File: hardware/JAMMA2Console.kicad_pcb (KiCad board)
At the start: 2 copper layers, 118 x 87.8 mm, 67 parts, among them J1 Conn_02x28_JAMMA, J2 SCART-F, J3 DB15_Female_HighDensity, J4 Conn_Coaxial_x2, J5 DB15_Female, J6 DB15_Female, J7 DF1BZ-34DP-2.5DSA, U1 STM32F103V8Tx, U2 74LVC4245, U3 74LVC4245, U4 74LVC4245, U5 LM1881, U6 TL072

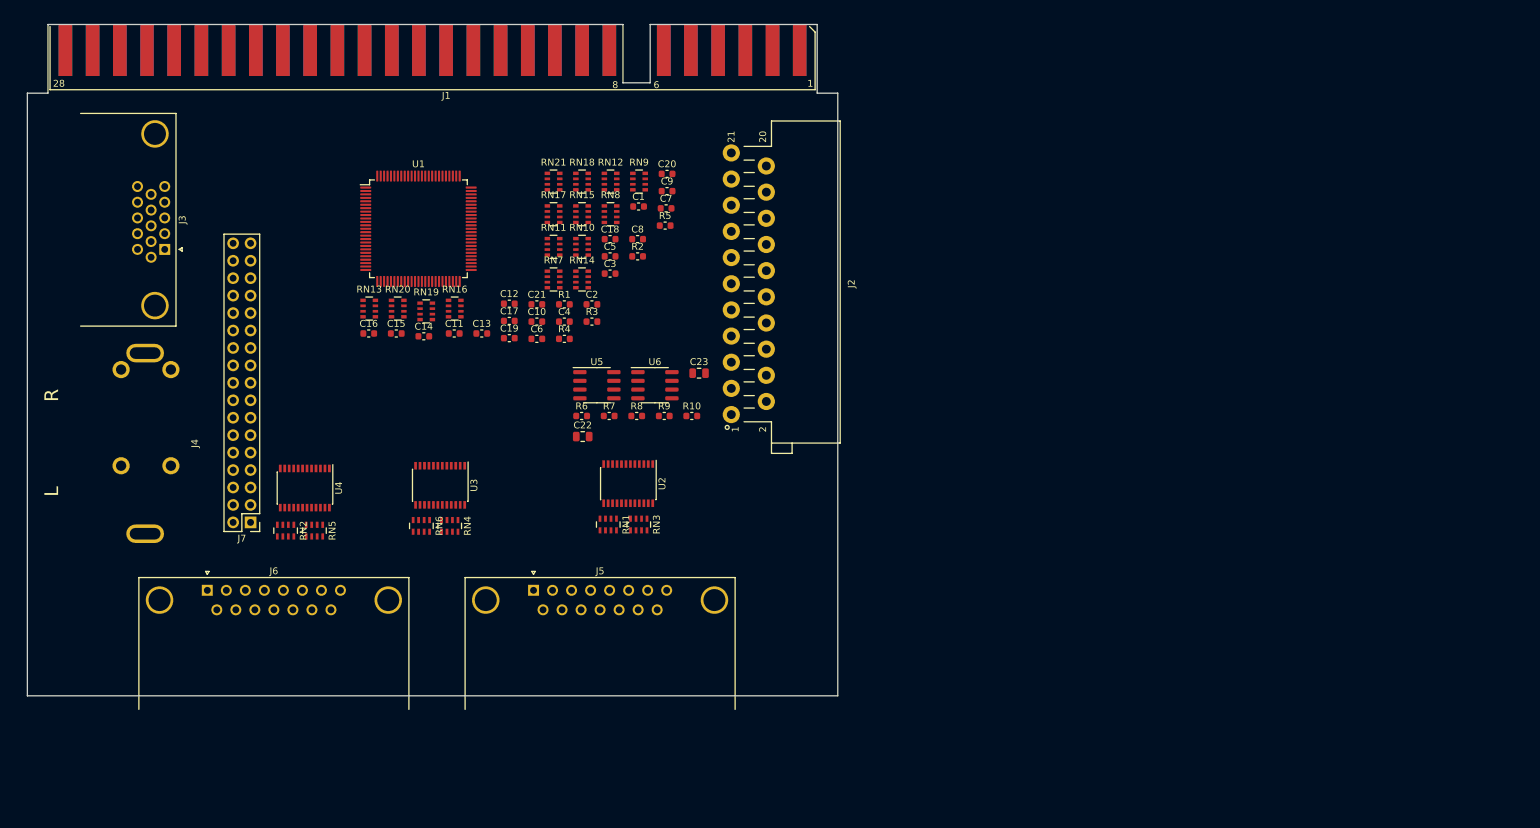
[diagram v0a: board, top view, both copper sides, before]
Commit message: More work on various schematic files, added footprint for the speaker out terminal connectors.
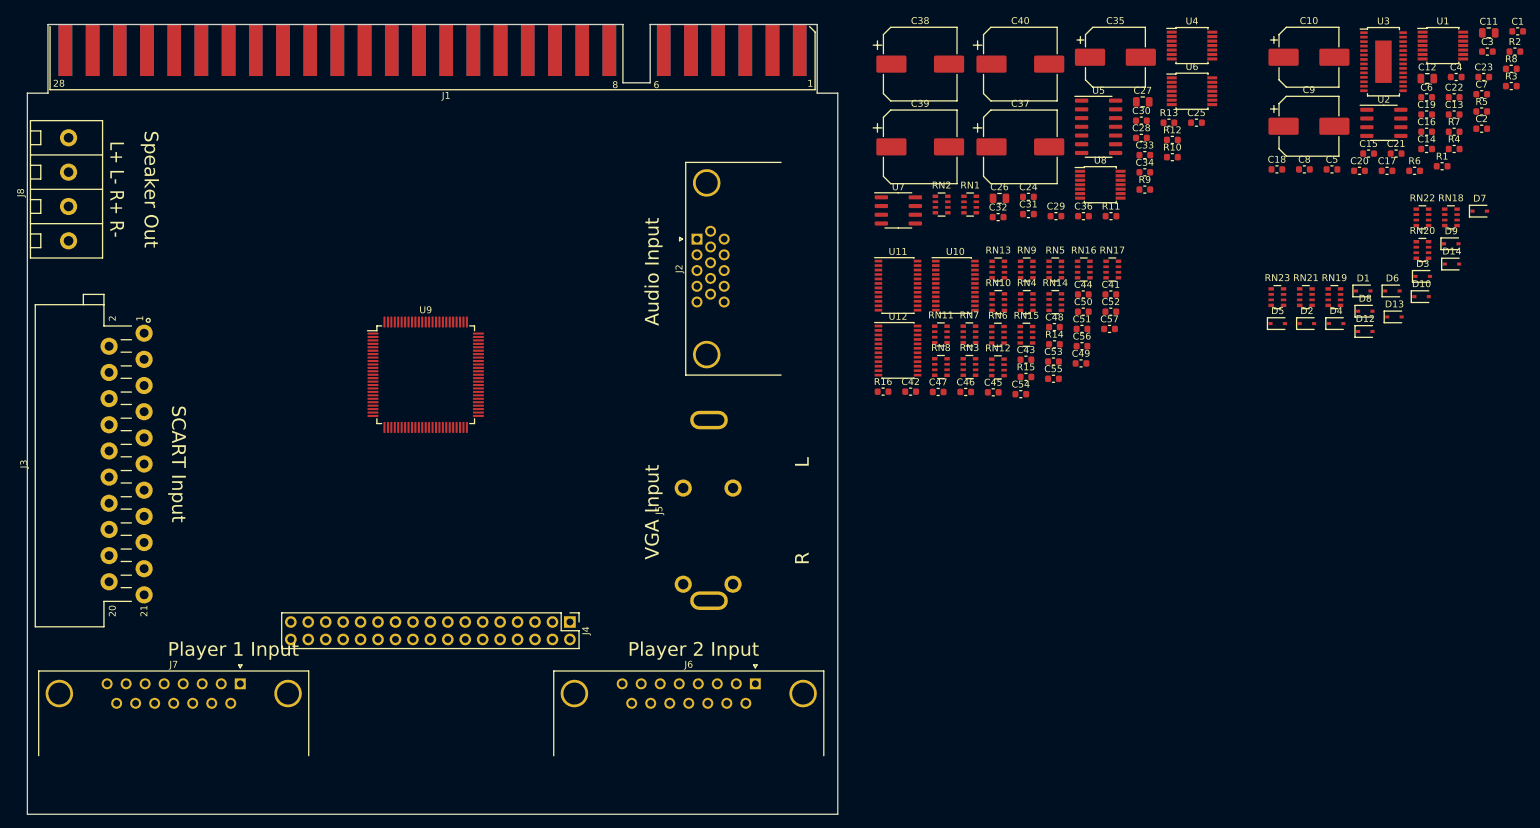
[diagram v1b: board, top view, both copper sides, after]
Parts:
- added C24: 100n, Capacitor_SMD:C_0603_1608Metric, F.Cu at (235.8, 69.3)
- added C25: 100n, Capacitor_SMD:C_0603_1608Metric, F.Cu at (260.2, 58.5)
- added C26: 10u, Capacitor_SMD:C_0805_2012Metric, F.Cu at (231.6, 69.6)
- added C27: 10u, Capacitor_SMD:C_0805_2012Metric, F.Cu at (252.4, 55.5)
- added C28: 100n, Capacitor_SMD:C_0603_1608Metric, F.Cu at (252.2, 60.8)
- added C29: 100n, Capacitor_SMD:C_0603_1608Metric, F.Cu at (239.8, 72.2)
- added C30: 100n, Capacitor_SMD:C_0603_1608Metric, F.Cu at (252.2, 58.2)
- added C31: 510p, Capacitor_SMD:C_0603_1608Metric, F.Cu at (235.8, 71.9)
- added C32: 100n, Capacitor_SMD:C_0603_1608Metric, F.Cu at (231.3, 72.3)
- added C33: 100n, Capacitor_SMD:C_0603_1608Metric, F.Cu at (252.7, 63.3)
- added C34: 100n, Capacitor_SMD:C_0603_1608Metric, F.Cu at (252.7, 65.8)
- added C35: 100u, Capacitor_SMD:CP_Elec_8x10.5, F.Cu at (248.4, 49.0)
- added C36: 100n, Capacitor_SMD:C_0603_1608Metric, F.Cu at (243.8, 72.2)
- added C37: 330u, Capacitor_SMD:CP_Elec_10x10.5, F.Cu at (234.6, 62.1)
- added C38: 330u, Capacitor_SMD:CP_Elec_10x10.5, F.Cu at (220.0, 50.0)
- added C39: 330u, Capacitor_SMD:CP_Elec_10x10.5, F.Cu at (220.0, 62.1)
- added C40: 330u, Capacitor_SMD:CP_Elec_10x10.5, F.Cu at (234.6, 50.0)
- added C41: 10u, Capacitor_SMD:C_0603_1608Metric, F.Cu at (247.8, 83.6)
- added C42: 100n, Capacitor_SMD:C_0603_1608Metric, F.Cu at (218.6, 97.7)
- added C43: 100n, Capacitor_SMD:C_0603_1608Metric, F.Cu at (235.4, 93.1)
- added C44: 100n, Capacitor_SMD:C_0603_1608Metric, F.Cu at (243.8, 83.6)
- added C45: 100n, Capacitor_SMD:C_0603_1608Metric, F.Cu at (230.6, 97.8)
- added C46: 100n, Capacitor_SMD:C_0603_1608Metric, F.Cu at (226.6, 97.8)
- added C47: 100n, Capacitor_SMD:C_0603_1608Metric, F.Cu at (222.6, 97.8)
- added C48: 10u, Capacitor_SMD:C_0603_1608Metric, F.Cu at (239.6, 88.3)
- added C49: 100n, Capacitor_SMD:C_0603_1608Metric, F.Cu at (243.4, 93.6)
- added C50: 100n, Capacitor_SMD:C_0603_1608Metric, F.Cu at (243.8, 86.1)
- added C51: 100n, Capacitor_SMD:C_0603_1608Metric, F.Cu at (243.6, 88.6)
- added C52: 100n, Capacitor_SMD:C_0603_1608Metric, F.Cu at (247.8, 86.1)
- added C53: 100n, Capacitor_SMD:C_0603_1608Metric, F.Cu at (239.4, 93.3)
- added C54: 100n, Capacitor_SMD:C_0603_1608Metric, F.Cu at (234.7, 98.1)
- added C55: 100n, Capacitor_SMD:C_0603_1608Metric, F.Cu at (239.4, 95.8)
- added C56: 100n, Capacitor_SMD:C_0603_1608Metric, F.Cu at (243.6, 91.1)
- added C57: 100n, Capacitor_SMD:C_0603_1608Metric, F.Cu at (247.6, 88.6)
- added D1: LESD3Z5.0CMT1G, Diode_SMD:D_SOD-323, F.Cu at (284.5, 83.0)
- added D10: LESD3Z5.0CMT1G, Diode_SMD:D_SOD-323, F.Cu at (293.0, 83.9)
- added D12: LESD3Z5.0CMT1G, Diode_SMD:D_SOD-323, F.Cu at (284.8, 89.0)
- added D13: LESD3Z5.0CMT1G, Diode_SMD:D_SOD-323, F.Cu at (289.1, 86.8)
- added D14: LESD3Z5.0CMT1G, Diode_SMD:D_SOD-323, F.Cu at (297.4, 79.1)
- added D2: LESD3Z5.0CMT1G, Diode_SMD:D_SOD-323, F.Cu at (276.3, 87.8)
- added D3: LESD3Z5.0CMT1G, Diode_SMD:D_SOD-323, F.Cu at (293.2, 80.9)
- added D4: LESD3Z5.0CMT1G, Diode_SMD:D_SOD-323, F.Cu at (280.6, 87.8)
- added D5: LESD3Z5.0CMT1G, Diode_SMD:D_SOD-323, F.Cu at (272.1, 87.8)
- added D6: LESD3Z5.0CMT1G, Diode_SMD:D_SOD-323, F.Cu at (288.8, 83.0)
- added D7: LESD3Z5.0CMT1G, Diode_SMD:D_SOD-323, F.Cu at (301.5, 71.4)
- added D8: LESD3Z5.0CMT1G, Diode_SMD:D_SOD-323, F.Cu at (284.8, 86.0)
- added D9: LESD3Z5.0CMT1G, Diode_SMD:D_SOD-323, F.Cu at (297.3, 76.2)
- added J8: Conn_01x04, Console2JAMMA:PhoenixContact_PTS_1,5_4-5_1x4_P5.00mm_Horizontal, F.Cu at (96.0, 68.2)
- added R11: 620, Resistor_SMD:R_0603_1608Metric, F.Cu at (247.8, 72.2)
- added R12: 680k, Resistor_SMD:R_0603_1608Metric, F.Cu at (256.7, 61.1)
- added R13: 10K, Resistor_SMD:R_0603_1608Metric, F.Cu at (256.2, 58.5)
- added R14: 10k, Resistor_SMD:R_0603_1608Metric, F.Cu at (239.6, 90.8)
- added R15: 10k, Resistor_SMD:R_0603_1608Metric, F.Cu at (235.4, 95.6)
- added R16: 10k, Resistor_SMD:R_0603_1608Metric, F.Cu at (214.6, 97.7)
- added RN22: 4K7, Resistor_SMD:R_Array_Convex_4x0603, F.Cu at (293.1, 72.3)
- added RN23: 4K7, Resistor_SMD:R_Array_Convex_4x0603, F.Cu at (272.0, 84.0)
- added U10: 74LVC4245, Package_SO:TSSOP-24_4.4x7.8mm_P0.65mm, F.Cu at (225.1, 82.3)
- added U11: 74LVC4245, Package_SO:TSSOP-24_4.4x7.8mm_P0.65mm, F.Cu at (216.8, 82.3)
- added U12: 74LVC4245, Package_SO:TSSOP-24_4.4x7.8mm_P0.65mm, F.Cu at (216.8, 91.7)
- added U7: LM1881, Package_SO:SOIC-8_3.9x4.9mm_P1.27mm, F.Cu at (216.8, 71.3)
- added U8: THS7375, Package_SO:TSSOP-14_4.4x5mm_P0.65mm, F.Cu at (246.2, 67.6)
- added U9: STM32F103V8Tx, Package_QFP:LQFP-100_14x14mm_P0.5mm, F.Cu at (148.0, 95.2)
- C1: value 510p -> 1u0
- C10, C9: value 100n -> 100u; footprint Capacitor_SMD:C_0603_1608Metric -> Capacitor_SMD:CP_Elec_8x10.5
- C11: value 100n -> 10u; footprint Capacitor_SMD:C_0603_1608Metric -> Capacitor_SMD:C_0805_2012Metric
- C12: footprint Capacitor_SMD:C_0603_1608Metric -> Capacitor_SMD:C_0805_2012Metric
- C15, C16, C19, C2, C3, C6, C7: value 100n -> 1u0
- C17, C18: value 100n -> 1n0
- C20, C21, C4, C8: value 100n -> 10n
- C22, C23: value 10u -> 10n; footprint Capacitor_SMD:C_0805_2012Metric -> Capacitor_SMD:C_0603_1608Metric
- C5: value 10u -> 1u0
- J2: value SCART-F -> DB15_Female_HighDensity; footprint Console2JAMMA:Conn_SCART_Female -> Connector_Dsub:DSUB-15-HD_Female_Horizontal_P2.29x1.98mm_EdgePinOffset8.35mm_Housed_MountingHolesOffset10.89mm
- J3: value DB15_Female_HighDensity -> SCART-F; footprint Connector_Dsub:DSUB-15-HD_Female_Horizontal_P2.29x1.98mm_EdgePinOffset8.35mm_Housed_MountingHolesOffset10.89mm -> Console2JAMMA:Conn_SCART_Female
- J4: value Conn_Coaxial_x2 -> DF1BZ-34DP-2.5DSA; footprint Console2JAMMA:RCA_Switchchraft_Dual -> Connector_PinHeader_2.54mm:PinHeader_2x17_P2.54mm_Vertical
- J5: value DB15_Female -> Conn_Coaxial_x2; footprint Connector_Dsub:DSUB-15_Male_Horizontal_P2.77x2.84mm_EdgePinOffset14.56mm_Housed_MountingHolesOffset15.98mm -> Console2JAMMA:RCA_Switchchraft_Dual
- J6: footprint Connector_Dsub:DSUB-15_Male_Horizontal_P2.77x2.84mm_EdgePinOffset14.56mm_Housed_MountingHolesOffset15.98mm -> Connector_Dsub:DSUB-15_Female_Horizontal_P2.77x2.84mm_EdgePinOffset7.70mm_Housed_MountingHolesOffset9.12mm
- J7: value DF1BZ-34DP-2.5DSA -> DB15_Female; footprint Connector_PinHeader_2.54mm:PinHeader_2x17_P2.54mm_Vertical -> Connector_Dsub:DSUB-15_Female_Horizontal_P2.77x2.84mm_EdgePinOffset7.70mm_Housed_MountingHolesOffset9.12mm
- R1: value 620 -> R_Small
- R10, R9: value 100K -> 4K7
- R2: value 680k -> R_Small
- R3, R4: value 10k -> 100K
- R5: value 10k -> 47K
- R8: value 47K -> 10K
- RN1, RN2: value 100R -> 75R; footprint Resistor_SMD:R_Array_Concave_4x0603 -> Resistor_SMD:R_Array_Convex_4x0603
- RN18, RN19, RN20, RN21: value 10k -> 4K7
- RN3, RN4, RN5, RN6: value 100R -> 10k; footprint Resistor_SMD:R_Array_Concave_4x0603 -> Resistor_SMD:R_Array_Convex_4x0603
- U1: value STM32F103V8Tx -> 74HC4053; footprint Package_QFP:LQFP-100_14x14mm_P0.5mm -> Package_SO:TSSOP-14_4.4x5mm_P0.65mm
- U2: value 74LVC4245 -> TL072; footprint Package_SO:TSSOP-24_4.4x7.8mm_P0.65mm -> Package_SO:SOIC-8_3.9x4.9mm_P1.27mm
- U3: value 74LVC4245 -> IS31AP2110; footprint Package_SO:TSSOP-24_4.4x7.8mm_P0.65mm -> Package_SO:TSSOP-28-1EP_4.4x9.7mm_P0.65mm
- U4: value 74LVC4245 -> 74HC4053; footprint Package_SO:TSSOP-24_4.4x7.8mm_P0.65mm -> Package_SO:TSSOP-14_4.4x5mm_P0.65mm
- U5: value LM1881 -> 74HC86; footprint Package_SO:SOIC-8_3.9x4.9mm_P1.27mm -> Package_SO:SOIC-14_3.9x8.7mm_P1.27mm
- U6: value TL072 -> 74HC4053; footprint Package_SO:SOIC-8_3.9x4.9mm_P1.27mm -> Package_SO:TSSOP-14_4.4x5mm_P0.65mm
- moved C11 156.9 mm to (302.8, 45.5)
- moved C16 156.8 mm to (293.7, 59.9)
- moved U1 151.5 mm to (296.1, 47.3)
- moved U3 150.6 mm to (287.5, 49.7), turned to 0 degrees
- moved RN20 149.4 mm to (293.1, 77.1)
- moved C14 148.5 mm to (293.7, 62.4)
- moved C13 145.1 mm to (297.8, 57.4)
- moved U4 144.4 mm to (259.6, 47.3), turned to 0 degrees
- moved C15 144.0 mm to (285.3, 63.0)
- moved R3 138.2 mm to (306.1, 53.2)
- moved C12 137.6 mm to (293.8, 52.1)
- moved C19 137.5 mm to (293.7, 57.4)
- moved R8 137.0 mm to (306.1, 50.7)
- moved C22 136.2 mm to (297.8, 54.9)
- moved C4 134.7 mm to (298.1, 51.9)
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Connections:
- net /Audio_R renamed /Speaker_R-
- net /P1P2_Shifter_DIR renamed Net-(U3-Pad2)
- net Net-(U1-Pad9) renamed /Audio/Audio_Select_Mono
- C1 pad 2: GND -> /Audio/EXT_Audio_L
- C10 pad 1: +3V3 -> +12V
- C11 pad 1: +3V3 -> Net-(C11-Pad1)
- C11 pad 2: GND -> /Audio/Audio_L
- C12 pad 1: +3V3 -> Net-(C12-Pad1)
- C12 pad 2: GND -> /Audio/Audio_R
- C13 pad 1: +3V3 -> +12V
- C14 pad 1: +3V3 -> +12V
- C15 pad 1: +3V3 -> Net-(C15-Pad1)
- C16 pad 1: VCC -> Net-(C16-Pad1)
- C17 pad 1: VCC -> +12V
- C18 pad 1: VCC -> +12V
- C19 pad 1: VCC -> +12V
- C2 pad 2: Net-(C1-Pad1) -> /Audio/EXT_Audio_R
- C20 pad 1: VCC -> /Speaker_JAMMA+
- C21 pad 1: VCC -> GND
- C21 pad 2: GND -> /Speaker_JAMMA-
- C22 pad 1: Net-(C22-Pad1) -> /Speaker_R+
- C22 pad 2: /Audio_L -> GND
- C23 pad 1: Net-(C23-Pad1) -> GND
- C3 pad 2: GND -> /Audio/Audio_Mono
- C5 pad 1: +3V3 -> Net-(C5-Pad1)
- C5 pad 2: GND -> /Audio/SCART_Audio_L
- C6 pad 1: +3V3 -> Net-(C6-Pad1)
- C6 pad 2: GND -> /Audio/SCART_Audio_R
- C7 pad 1: +3V3 -> Net-(C7-Pad1)
- C7 pad 2: GND -> /Audio/Audio_L
- C8 pad 1: +3V3 -> -5V
- C9 pad 1: +3V3 -> +12V
- J1 pad 10: /Speaker_R -> /Speaker_JAMMA+
- J1 pad L: /Speaker_L -> /Speaker_JAMMA-
- J2 pad 1: Net-(J2-Pad1) -> /VGA_Red
- J2 pad 10: Net-(J2-Pad10) -> GND
- J2 pad 11: /SCART_Green -> Net-(J2-Pad11)
- J2 pad 12: Net-(J2-Pad12) -> /VGA_SDA
- J2 pad 13: GND -> /VGA_HSYNC
- J2 pad 14: GND -> /VGA_VSYNC
- J2 pad 15: /SCART_Red -> /VGA_SCK
- J2 pad 2: /SCART_Audio_R -> /VGA_Green
- J2 pad 3: Net-(J2-Pad3) -> /VGA_Blue
- J2 pad 4: GND -> Net-(J2-Pad4)
- J2 pad 6: /SCART_Audio_L -> GND
- J2 pad 7: /SCART_Blue -> GND
- J2 pad 8: /SWITCH -> GND
- J2 pad 9: GND -> Net-(J2-Pad9)
- J3 pad 1: /VGA_Red -> Net-(J3-Pad1)
- J3 pad 10: GND -> Net-(J3-Pad10)
- J3 pad 11: Net-(J3-Pad11) -> /SCART_Green
- J3 pad 12: /VGA_SDA -> Net-(J3-Pad12)
- J3 pad 13: /VGA_HSYNC -> GND
- J3 pad 14: /VGA_VSYNC -> GND
- J3 pad 15: /VGA_SCK -> /SCART_Red
- J3 pad 2: /VGA_Green -> /SCART_Audio_R
- J3 pad 3: /VGA_Blue -> Net-(J3-Pad3)
- J3 pad 4: Net-(J3-Pad4) -> GND
- J3 pad 6: GND -> /SCART_Audio_L
- J3 pad 7: GND -> /SCART_Blue
- J3 pad 8: GND -> /SCART_Switch
- J3 pad 9: Net-(J3-Pad9) -> GND
- J4 pad 3: GND -> Net-(J4-Pad3)
- J5 pad 1: GND -> /EXT_Audio_L
- J5 pad 2: Net-(J5-Pad2) -> /EXT_Audio_R
- J5 pad 3: Net-(J5-Pad3) -> GND
- J6 pad 1: GND -> /Digital I/O/VCC
- J6 pad 15: Net-(J6-Pad15) -> GND
- J6 pad 8: VCC -> GND
- J6 pad 9: GND -> Net-(J6-Pad9)
- J7 pad 1: Net-(J7-Pad1) -> /Digital I/O/VCC
- J7 pad 15: /P1_HK -> GND
- J7 pad 8: Net-(J7-Pad8) -> GND
- J7 pad 9: /P2_HK -> Net-(J7-Pad9)
- R1 pad 1: Net-(C1-Pad1) -> +12V
- R1 pad 2: /SCART_COMP -> Net-(R1-Pad2)
- R10 pad 1: /Audio_Mono -> Net-(C27-Pad1)
- R10 pad 2: Net-(R10-Pad2) -> /Video/VGA_VSYNC
- R2 pad 1: Net-(C3-Pad1) -> Net-(R1-Pad2)
- R3 pad 1: GND -> Net-(R3-Pad1)
- R3 pad 2: Net-(R3-Pad2) -> Net-(C11-Pad1)
- R4 pad 1: GND -> Net-(R3-Pad1)
- R4 pad 2: Net-(R4-Pad2) -> Net-(C12-Pad1)
- R5 pad 1: GND -> Net-(R5-Pad1)
- R5 pad 2: Net-(R5-Pad2) -> Net-(R3-Pad1)
- R6 pad 2: Net-(C22-Pad1) -> Net-(R5-Pad1)
- R7 pad 1: Net-(R6-Pad1) -> Net-(R7-Pad1)
- R7 pad 2: Net-(C23-Pad1) -> Net-(R6-Pad1)
- R8 pad 1: Net-(R8-Pad1) -> /Audio/Audio_Mono
- R8 pad 2: Net-(R6-Pad1) -> Net-(R7-Pad1)
- R9 pad 1: Net-(R10-Pad2) -> Net-(C26-Pad1)
- R9 pad 2: Net-(R8-Pad1) -> /Video/VGA_HSYNC
- RN1 pad 1: Net-(RN1-Pad1) -> GND
- RN1 pad 2: Net-(RN1-Pad2) -> GND
- RN1 pad 3: Net-(RN1-Pad3) -> GND
- RN1 pad 4: Net-(RN1-Pad4) -> GND
- RN1 pad 5: Net-(J5-Pad4) -> /Video/Video_CSYNC
- RN1 pad 6: Net-(J5-Pad12) -> /Video/Video_Blue
- RN1 pad 7: Net-(J5-Pad5) -> /Video/Video_Green
- RN1 pad 8: Net-(J5-Pad13) -> /Video/Video_Red
- RN10 pad 1: /P1_HK -> /P2_HK
- RN10 pad 2: /P1_MK -> /P2_MK
- RN10 pad 3: /P1_LK -> /P2_LK
- RN11 pad 1: /Coin_B -> Net-(RN11-Pad1)
- RN11 pad 2: /P2_Start -> Net-(RN11-Pad2)
- RN11 pad 3: /P2_Up -> Net-(RN11-Pad3)
- RN11 pad 4: /P2_Down -> Net-(RN11-Pad4)
- RN11 pad 5: Net-(RN11-Pad5) -> /Digital I/O/P1_Button4
- RN11 pad 6: Net-(RN11-Pad6) -> /Digital I/O/P1_Button3
- RN11 pad 7: Net-(RN11-Pad7) -> /Digital I/O/P1_Button2
- RN11 pad 8: Net-(RN11-Pad8) -> /Digital I/O/P1_Button1
- RN12 pad 1: /P2_Left -> Net-(RN12-Pad1)
- RN12 pad 2: /P2_Right -> Net-(RN12-Pad2)
- RN12 pad 3: /P2_A -> Net-(RN12-Pad3)
- RN12 pad 4: /P2_B -> Net-(RN12-Pad4)
- RN12 pad 5: Net-(RN12-Pad5) -> /Digital I/O/P1_Button8
- RN12 pad 6: Net-(RN12-Pad6) -> /Digital I/O/P1_Button7
- RN12 pad 7: Net-(RN12-Pad7) -> /Digital I/O/P1_Button6
- RN12 pad 8: Net-(RN12-Pad8) -> /Digital I/O/P1_Button5
- RN13 pad 1: /P2_C -> Net-(RN13-Pad1)
- RN13 pad 2: /P2_X -> Net-(RN13-Pad2)
- RN13 pad 3: /P2_Y -> Net-(RN13-Pad3)
- RN13 pad 4: /P2_Z -> Net-(RN13-Pad4)
- RN13 pad 5: Net-(RN13-Pad5) -> /Digital I/O/P1_Button12
- RN13 pad 6: Net-(RN13-Pad6) -> /Digital I/O/P1_Button11
- RN13 pad 7: Net-(RN13-Pad7) -> /Digital I/O/P1_Button10
- RN13 pad 8: Net-(RN13-Pad8) -> /Digital I/O/P1_Button9
- RN14 pad 1: /P2_HK -> Net-(RN14-Pad1)
- RN14 pad 2: /P2_MK -> Net-(RN14-Pad2)
- RN14 pad 3: /P2_LK -> Net-(RN14-Pad3)
- RN14 pad 4: GND -> Net-(RN14-Pad4)
- RN14 pad 5: Net-(RN14-Pad5) -> GND
- RN14 pad 6: Net-(RN14-Pad6) -> /Digital I/O/P2_Shifter_DIR
- RN14 pad 7: Net-(RN14-Pad7) -> /Digital I/O/P1&P2_Shifter_DIR
- RN14 pad 8: Net-(RN14-Pad8) -> /Digital I/O/P1_Shifter_DIR
- RN15 pad 5: /P1_Button4 -> /Digital I/O/P2_Button4
- RN15 pad 6: /P1_Button3 -> /Digital I/O/P2_Button3
- RN15 pad 7: /P1_Button2 -> /Digital I/O/P2_Button2
- RN15 pad 8: /P1_Button1 -> /Digital I/O/P2_Button1
- RN16 pad 5: /P1_Button8 -> /Digital I/O/P2_Button8
- RN16 pad 6: /P1_Button7 -> /Digital I/O/P2_Button7
- RN16 pad 7: /P1_Button6 -> /Digital I/O/P2_Button6
- RN16 pad 8: /P1_Button5 -> /Digital I/O/P2_Button5
- RN17 pad 5: /P1_Button12 -> /Digital I/O/P2_Button12
- RN17 pad 6: /P1_Button11 -> /Digital I/O/P2_Button11
- RN17 pad 7: /P1_Button10 -> /Digital I/O/P2_Button10
- RN17 pad 8: /P1_Button9 -> /Digital I/O/P2_Button9
- RN18 pad 1: Net-(RN18-Pad1) -> /Digital I/O/P1_1
- RN18 pad 2: Net-(RN18-Pad2) -> /Digital I/O/P1_2
- RN18 pad 3: Net-(RN18-Pad3) -> /Digital I/O/P1_3
- RN18 pad 4: Net-(RN18-Pad4) -> /Digital I/O/P1_4
- RN18 pad 5: GND -> Net-(J6-Pad3)
- RN18 pad 6: /P2_Shifter_DIR -> Net-(J6-Pad10)
- RN18 pad 7: /P1&P2_Shifter_DIR -> Net-(J6-Pad2)
- RN18 pad 8: /P1_Shifter_DIR -> Net-(J6-Pad9)
- RN19 pad 1: Net-(RN19-Pad1) -> /Digital I/O/P1_5
- RN19 pad 2: Net-(RN19-Pad2) -> /Digital I/O/P1_6
- RN19 pad 3: Net-(RN19-Pad3) -> /Digital I/O/P1_7
- RN19 pad 4: Net-(RN19-Pad4) -> /Digital I/O/P1_8
- RN19 pad 5: /P2_Button4 -> Net-(J6-Pad5)
- RN19 pad 6: /P2_Button3 -> Net-(J6-Pad12)
- RN19 pad 7: /P2_Button2 -> Net-(J6-Pad4)
- RN19 pad 8: /P2_Button1 -> Net-(J6-Pad11)
- RN2 pad 5: Net-(J6-Pad4) -> Net-(C40-Pad1)
- RN2 pad 6: Net-(J6-Pad12) -> Net-(C38-Pad1)
- RN2 pad 7: Net-(J6-Pad5) -> Net-(C39-Pad1)
- RN2 pad 8: Net-(J6-Pad13) -> Net-(C37-Pad1)
- RN20 pad 1: Net-(RN20-Pad1) -> /Digital I/O/P1_9
- RN20 pad 2: Net-(RN20-Pad2) -> /Digital I/O/P1_10
- RN20 pad 3: Net-(RN20-Pad3) -> /Digital I/O/P1_11
- RN20 pad 4: Net-(RN20-Pad4) -> /Digital I/O/P1_12
- RN20 pad 5: /P2_Button8 -> Net-(J6-Pad7)
- RN20 pad 6: /P2_Button7 -> Net-(J6-Pad14)
- RN20 pad 7: /P2_Button6 -> Net-(J6-Pad6)
- RN20 pad 8: /P2_Button5 -> Net-(J6-Pad13)
- RN21 pad 1: Net-(RN21-Pad1) -> /Digital I/O/P2_1
- RN21 pad 2: Net-(RN21-Pad2) -> /Digital I/O/P2_2
- RN21 pad 3: Net-(RN21-Pad3) -> /Digital I/O/P2_3
- RN21 pad 4: Net-(RN21-Pad4) -> /Digital I/O/P2_4
- RN21 pad 5: /P2_Button12 -> Net-(J7-Pad3)
- RN21 pad 6: /P2_Button11 -> Net-(J7-Pad10)
- RN21 pad 7: /P2_Button10 -> Net-(J7-Pad2)
- RN21 pad 8: /P2_Button9 -> Net-(J7-Pad9)
- RN3 pad 1: Net-(RN3-Pad1) -> /Coin_A
- RN3 pad 2: Net-(RN3-Pad2) -> /P1_Start
- RN3 pad 3: Net-(RN3-Pad3) -> /P1_Up
- RN3 pad 4: Net-(RN3-Pad4) -> /P1_Down
- RN3 pad 5: Net-(J5-Pad6) -> Net-(RN3-Pad5)
- RN3 pad 6: Net-(J5-Pad14) -> Net-(RN3-Pad6)
- RN3 pad 7: Net-(J5-Pad7) -> Net-(RN3-Pad7)
- RN3 pad 8: Net-(J5-Pad15) -> Net-(RN3-Pad8)
- RN4 pad 1: Net-(RN4-Pad1) -> /P1_Left
- RN4 pad 2: Net-(RN4-Pad2) -> /P1_Right
- RN4 pad 3: Net-(RN4-Pad3) -> /P1_A
- RN4 pad 4: Net-(RN4-Pad4) -> /P1_B
- RN4 pad 5: Net-(J5-Pad2) -> Net-(RN4-Pad5)
- RN4 pad 6: Net-(J5-Pad10) -> Net-(RN4-Pad6)
- RN4 pad 7: Net-(J5-Pad3) -> Net-(RN4-Pad7)
- RN4 pad 8: Net-(J5-Pad11) -> Net-(RN4-Pad8)
- RN5 pad 1: Net-(RN5-Pad1) -> /P1_C
- RN5 pad 2: Net-(RN5-Pad2) -> /P1_X
- RN5 pad 3: Net-(RN5-Pad3) -> /P1_Y
- RN5 pad 4: Net-(RN5-Pad4) -> /P1_Z
- RN5 pad 5: Net-(J6-Pad6) -> Net-(RN5-Pad5)
- RN5 pad 6: Net-(J6-Pad14) -> Net-(RN5-Pad6)
- RN5 pad 7: Net-(J6-Pad7) -> Net-(RN5-Pad7)
- RN5 pad 8: Net-(J6-Pad15) -> Net-(RN5-Pad8)
- RN6 pad 1: Net-(RN6-Pad1) -> /P1_HK
- RN6 pad 2: Net-(RN6-Pad2) -> /P1_MK
- RN6 pad 3: Net-(RN6-Pad3) -> /P1_LK
- RN6 pad 4: Net-(RN6-Pad4) -> GND
- RN6 pad 5: Net-(J6-Pad2) -> Net-(RN6-Pad5)
- RN6 pad 6: Net-(J6-Pad10) -> Net-(RN6-Pad6)
- RN6 pad 7: Net-(J6-Pad3) -> Net-(RN6-Pad7)
- RN6 pad 8: Net-(J6-Pad11) -> Net-(RN6-Pad8)
- RN7 pad 1: /Coin_A -> /Coin_B
- RN7 pad 2: /P1_Start -> /P2_Start
- RN7 pad 3: /P1_Up -> /P2_Up
- RN7 pad 4: /P1_Down -> /P2_Down
- RN8 pad 1: /P1_Left -> /P2_Left
- RN8 pad 2: /P1_Right -> /P2_Right
- RN8 pad 3: /P1_A -> /P2_A
- RN8 pad 4: /P1_B -> /P2_B
- RN9 pad 1: /P1_C -> /P2_C
- RN9 pad 2: /P1_X -> /P2_X
- RN9 pad 3: /P1_Y -> /P2_Y
- RN9 pad 4: /P1_Z -> /P2_Z
- U1 pad 1: Net-(RN7-Pad6) -> Net-(C2-Pad1)
- U1 pad 10: GND -> /Audio/Audio_Select_R
- U1 pad 11: +3V3 -> /Audio/Audio_Select_L
- U1 pad 12: Net-(U1-Pad12) -> Net-(C5-Pad1)
- U1 pad 13: Net-(U1-Pad13) -> Net-(C1-Pad1)
- U1 pad 14: Net-(U1-Pad14) -> /Audio/Audio_R
- U1 pad 2: Net-(RN7-Pad5) -> Net-(C6-Pad1)
- U1 pad 3: Net-(RN8-Pad8) -> Net-(C3-Pad1)
- U1 pad 4: Net-(RN8-Pad7) -> /Audio/Audio_L_OR_Mono
- U1 pad 5: Net-(RN8-Pad6) -> Net-(C7-Pad1)
- U1 pad 6: Net-(U1-Pad6) -> GND
- U1 pad 7: Net-(U1-Pad7) -> -5V
- U1 pad 8: Net-(U1-Pad8) -> GND
- U2 pad 1: +3V3 -> Net-(R5-Pad1)
- U2 pad 2: /P1_Shifter_DIR -> Net-(R3-Pad1)
- U2 pad 3: /P1_Button1 -> GND
- U2 pad 4: /P1_Button2 -> -12V
- U2 pad 5: /P1_Button3 -> GND
- U2 pad 6: /P1_Button4 -> Net-(R6-Pad1)
- U2 pad 7: /P1_Button5 -> Net-(R7-Pad1)
- U2 pad 8: /P1_Button6 -> +12V
- U3 pad 1: +3V3 -> Net-(U3-Pad1)
- U3 pad 10: /P2_Button12 -> Net-(R1-Pad2)
- U3 pad 11: GND -> Net-(C16-Pad1)
- U3 pad 12: GND -> /Audio/Audio_R
- U3 pad 13: GND -> Net-(U3-Pad13)
- U3 pad 14: Net-(RN6-Pad4) -> GND
- U3 pad 15: Net-(RN6-Pad3) -> +12V
- U3 pad 16: Net-(RN6-Pad2) -> +12V
- U3 pad 17: Net-(RN6-Pad1) -> Net-(U3-Pad13)
- U3 pad 18: Net-(RN4-Pad4) -> Net-(L3-Pad1)
- U3 pad 19: Net-(RN4-Pad3) -> GND
- U3 pad 20: Net-(RN4-Pad2) -> Net-(L4-Pad1)
- U3 pad 21: Net-(RN4-Pad1) -> Net-(U3-Pad13)
- U3 pad 22: Net-(R4-Pad2) -> Net-(U3-Pad13)
- U3 pad 23: VCC -> Net-(L2-Pad1)
- U3 pad 24: VCC -> GND
- U3 pad 3: /P1_Button9 -> /Audio/Audio_L_OR_Mono
- U3 pad 4: /P1_Button10 -> Net-(C15-Pad1)
- U3 pad 5: /P1_Button11 -> GND
- U3 pad 6: /P1_Button12 -> GND
- U3 pad 7: /P2_Button9 -> Net-(U3-Pad13)
- U3 pad 8: /P2_Button10 -> GND
- U3 pad 9: /P2_Button11 -> +12V
- U4 pad 1: +3V3 -> /Video/VGA_Green
- U4 pad 10: /P2_Button8 -> /Video/Video_Select_Green
- U4 pad 11: GND -> /Video/Video_Select_Red
- U4 pad 12: GND -> /Video/SCART_Red
- U4 pad 13: GND -> /Video/VGA_Red
- U4 pad 14: Net-(RN2-Pad4) -> /Video/Video_Green
- U4 pad 2: /P2_Shifter_DIR -> /Video/SCART_Green
- U4 pad 3: /P2_Button1 -> /Video/VGA_Blue
- U4 pad 4: /P2_Button2 -> /Video/Video_Blue
- U4 pad 5: /P2_Button3 -> /Video/SCART_Blue
- U4 pad 6: /P2_Button4 -> GND
- U4 pad 7: /P2_Button5 -> -5V
- U4 pad 8: /P2_Button6 -> GND
- U4 pad 9: /P2_Button7 -> /Video/Video_Select_Blue
- U5 pad 1: /SCART_CSYNC -> /Video/VGA_HSYNC
- U5 pad 2: Net-(C2-Pad1) -> Net-(C26-Pad1)
- U5 pad 4: GND -> /Video/VGA_VSYNC
- U5 pad 5: Net-(U5-Pad5) -> Net-(C27-Pad1)
- U5 pad 6: Net-(C3-Pad1) -> Net-(U5-Pad10)
- U5 pad 7: Net-(U5-Pad7) -> GND
- U5 pad 8: +5V -> Net-(U5-Pad13)
- U6 pad 1: Net-(R8-Pad1) -> GND
- U6 pad 2: Net-(R6-Pad1) -> GND
- U6 pad 4: -12V -> Net-(U6-Pad4)
- U6 pad 6: Net-(R10-Pad2) -> GND
- U6 pad 7: /Audio_Mono -> -5V
- U6 pad 8: +12V -> GND
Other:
- board size 118 x 87.8 mm -> 118 x 105 mm
- board text added: "Audio Input"
- board text added: "L+ L- R+ R-"
- board text added: "Player 1 Input"
- board text added: "Player 2 Input"
- board text added: "SCART Input"
- board text added: "Speaker Out"
- board text added: "VGA Input"
